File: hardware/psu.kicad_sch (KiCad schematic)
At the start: 58 parts, among them IC1 TLV61220DBVT, J2 Conn_01x03, J6 Barrel_Jack_Switch, Q3 CSD87503Q3E, Q4 CSD87503Q3E, U4 TPS63020DSJR, U5 BQ25798RQMR

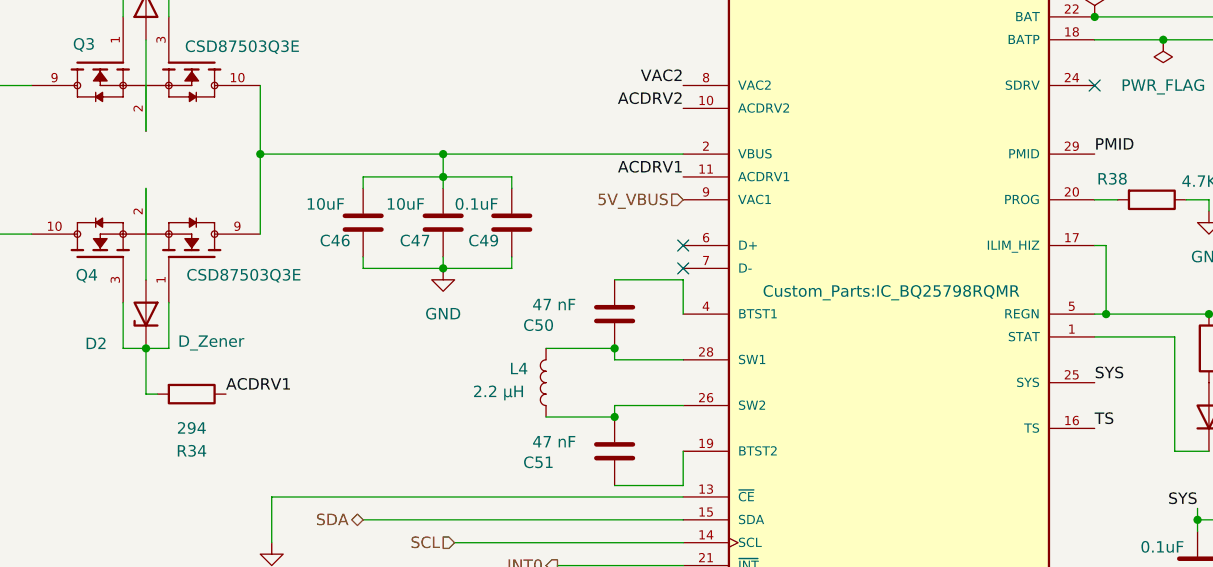
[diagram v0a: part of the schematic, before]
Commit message: updated major symbol and footprints
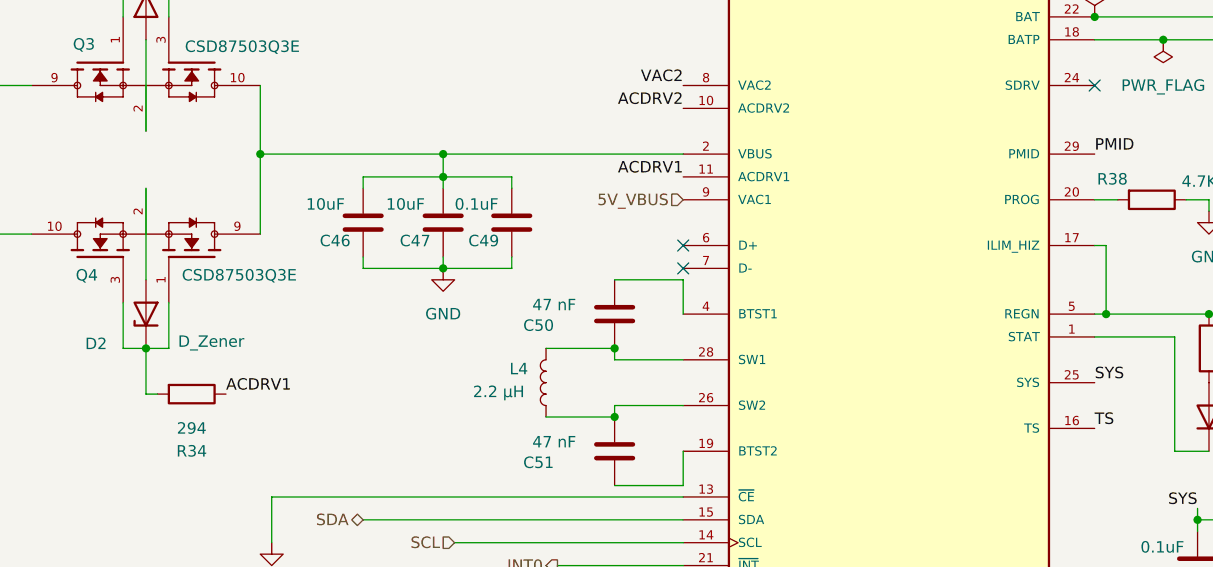
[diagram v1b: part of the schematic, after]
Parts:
- IC1: footprint (none) -> pyronet_footprints:SOT95P280X110-6; symbol TLV61220DBVT:TLV61220DBVT -> pyronet_symbols:TLV61220DBVT; Purchase-URL (none) -> https://www.snapeda.com/api/url_track_click_mouser/?unipart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
- Q3, Q4: footprint Custom_Parts:TRANS_CSD87503Q3E -> pyronet_footprints:TRANS_CSD87503Q3ET; symbol CSD87503Q3E:CSD87503Q3E -> pyronet_symbols:CSD87503Q3ET; Availability In Stock -> Warning; Check_prices https://www.snapeda.com/parts/CSD87503Q3E/Texas+Instruments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 -> https://www.snapeda.com/parts/CSD87503Q3ET/Texas+Instrument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; DigiKey_Part_Number (none) -> 296-47497-1-ND; MP CSD87503Q3E -> CSD87503Q3ET; Purchase-URL (none) -> https://www.snapeda.com/api/url_track_click_mouser/?unipart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; SnapEDA_Link https://www.snapeda.com/parts/CSD87503Q3E/Texas+Instruments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 -> https://www.snapeda.com/parts/CSD87503Q3ET/Texas+Instrument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
- U4: footprint TPS63020DSJR:IC_TPS63020DSJR -> pyronet_footprints:IC_TPS63020DSJR; symbol TPS63020DSJR:TPS63020DSJR -> pyronet_symbols:TPS63020DSJR; Purchase-URL (none) -> https://www.snapeda.com/api/url_track_click_mouser/?unipart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
- U5: footprint Custom_Parts:IC_BQ25798RQMR -> pyronet_footprints:IC_BQ25798RQMR; symbol BQ25798RQMR:BQ25798RQMR -> pyronet_symbols:BQ25798RQMR
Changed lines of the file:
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@@
 	)
 	(symbol
-		(lib_id "TLV61220DBVT:TLV61220DBVT")
+		(lib_id "pyronet_symbols:TLV61220DBVT")
 		(at 199.39 140.97 0)
 		(unit 1)
@@
 			)
 		)
-		(property "Footprint" ""
+		(property "Footprint" "pyronet_footprints:SOT95P280X110-6"
 			(at 199.39 140.97 0)
 			(effects
@@
 			)
 		)
-		(property "Description" ""
+		(property "Description" "Texas Instruments TLV61220DBVT, Boost Converter, Boost Converter 200mA Adjustable, 1.8  5.5 V, 6-Pin SOT-23"
 			(at 199.39 140.97 0)
 			(effects
@@
 					(size 1.27 1.27)
 				)
+				(justify bottom)
 				(hide yes)
 			)
@@
 			)
 		)
+		(property "Purchase-URL" "https://www.snapeda.com/api/url_track_click_mouser/?unipart_id=50780&manufacturer=Texas Instruments&part_name=TLV61220DBVT&search_term=  tlv61220dbvt"
+			(at 199.39 140.97 0)
+			(effects
+				(font
+					(size 1.27 1.27)
+				)
+				(justify bottom)
+				(hide yes)
+			)
+		)
 		(pin "6"
 		)
@@
 	)
 	(symbol
-		(lib_id "CSD87503Q3E:CSD87503Q3E")
+		(lib_name "CSD87503Q3ET_1")
+		(lib_id "pyronet_symbols:CSD87503Q3ET")
 		(at 71.12 33.02 0)
 		(unit 1)
@@
 			)
 		)
-		(property "Footprint" "Custom_Parts:TRANS_CSD87503Q3E"
+		(property "Footprint" "pyronet_footprints:TRANS_CSD87503Q3ET"
 			(at 71.12 33.02 0)
 			(effects
@@
 			)
 		)
-		(property "Check_prices" "https://www.snapeda.com/parts/CSD87503Q3E/Texas+Instruments/view-part/?ref=eda"
+		(property "Check_prices" "https://www.snapeda.com/parts/CSD87503Q3ET/Texas+Instruments/view-part/?ref=eda"
 			(at 71.12 33.02 0)
 			(effects
@@
 			)
 		)
-		(property "SnapEDA_Link" "https://www.snapeda.com/parts/CSD87503Q3E/Texas+Instruments/view-part/?ref=snap"
+		(property "SnapEDA_Link" "https://www.snapeda.com/parts/CSD87503Q3ET/Texas+Instruments/view-part/?ref=snap"
 			(at 71.12 33.02 0)
 			(effects
@@
 			)
 		)
-		(property "MP" "CSD87503Q3E"
+		(property "MP" "CSD87503Q3ET"
 			(at 71.12 33.02 0)
 			(effects
@@
 			)
 		)
-		(property "Availability" "In Stock"
+		(property "Availability" "Warning"
 			(at 71.12 33.02 0)
 			(effects
@@
 			)
 		)
+		(property "Purchase-URL" "https://www.snapeda.com/api/url_track_click_mouser/?unipart_id=1406469&manufacturer=Texas Instruments&part_name=CSD87503Q3ET&search_term=csd87503q3e"
+			(at 71.12 33.02 0)
+			(effects
+				(font
+					(size 1.27 1.27)
+				)
+				(justify bottom)
+				(hide yes)
+			)
+		)
+		(property "DigiKey_Part_Number" "296-47497-1-ND"
+			(at 71.12 33.02 0)
+			(effects
+				(font
+					(size 1.27 1.27)
+				)
+				(justify bottom)
+				(hide yes)
+			)
+		)
 		(pin "4"
 		)
@@
 	)
 	(symbol
-		(lib_id "CSD87503Q3E:CSD87503Q3E")
+		(lib_id "pyronet_symbols:CSD87503Q3ET")
 		(at 71.12 54.61 180)
 		(unit 1)
@@
 		)
 		(property "Value" "CSD87503Q3E"
-			(at 88.392 56.642 0)
+			(at 87.884 56.642 0)
 			(effects
 				(font
@@
 			)
 		)
-		(property "Footprint" "Custom_Parts:TRANS_CSD87503Q3E"
+		(property "Footprint" "pyronet_footprints:TRANS_CSD87503Q3ET"
 			(at 71.12 54.61 0)
 			(effects
@@
 			)
 		)
-		(property "Check_prices" "https://www.snapeda.com/parts/CSD87503Q3E/Texas+Instruments/view-part/?ref=eda"
+		(property "Check_prices" "https://www.snapeda.com/parts/CSD87503Q3ET/Texas+Instruments/view-part/?ref=eda"
 			(at 71.12 54.61 0)
 			(effects
@@
 			)
 		)
-		(property "SnapEDA_Link" "https://www.snapeda.com/parts/CSD87503Q3E/Texas+Instruments/view-part/?ref=snap"
+		(property "SnapEDA_Link" "https://www.snapeda.com/parts/CSD87503Q3ET/Texas+Instruments/view-part/?ref=snap"
 			(at 71.12 54.61 0)
 			(effects
@@
 			)
 		)
-		(property "MP" "CSD87503Q3E"
+		(property "MP" "CSD87503Q3ET"
 			(at 71.12 54.61 0)
 			(effects
@@
 			)
 		)
-		(property "Availability" "In Stock"
+		(property "Availability" "Warning"
 			(at 71.12 54.61 0)
 			(effects
@@
 			)
 		)
+		(property "Purchase-URL" "https://www.snapeda.com/api/url_track_click_mouser/?unipart_id=1406469&manufacturer=Texas Instruments&part_name=CSD87503Q3ET&search_term=csd87503q3e"
+			(at 71.12 54.61 0)
+			(effects
+				(font
+					(size 1.27 1.27)
+				)
+				(justify bottom)
+				(hide yes)
+			)
+		)
+		(property "DigiKey_Part_Number" "296-47497-1-ND"
+			(at 71.12 54.61 0)
+			(effects
+				(font
+					(size 1.27 1.27)
+				)
+				(justify bottom)
+				(hide yes)
+			)
+		)
 		(pin "4"
 		)
@@
 	)
 	(symbol
-		(lib_id "BQ25798RQMR:BQ25798RQMR")
+		(lib_id "pyronet_symbols:BQ25798RQMR")
 		(at 153.67 60.96 0)
 		(unit 1)
@@
 			)
 		)
-		(property "Footprint" "Custom_Parts:IC_BQ25798RQMR"
-			(at 153.924 59.182 0)
+		(property "Footprint" "pyronet_footprints:IC_BQ25798RQMR"
+			(at 153.67 60.96 0)
 			(effects
 				(font
@@
 				)
 				(justify bottom)
+				(hide yes)
 			)
 		)
@@
 	)
 	(symbol
-		(lib_id "TPS63020DSJR:TPS63020DSJR")
+		(lib_id "pyronet_symbols:TPS63020DSJR")
 		(at 57.15 152.4 0)
 		(unit 1)
@@
 			)
 		)
-		(property "Footprint" "TPS63020DSJR:IC_TPS63020DSJR"
+		(property "Footprint" "pyronet_footprints:IC_TPS63020DSJR"
 			(at 57.15 152.4 0)
 			(effects
@@
 			(at 57.15 152.4 0)
 			(effects
+				(font
+					(size 1.27 1.27)
+				)
+				(justify bottom)
+				(hide yes)
+			)
+		)
+		(property "Purchase-URL" "https://www.snapeda.com/api/url_track_click_mouser/?unipart_id=296571&manufacturer=Texas Instruments&part_name=TPS63020DSJR&search_term=tps63020dsjr"
+			(at 57.15 152.4 0)
+			(effects

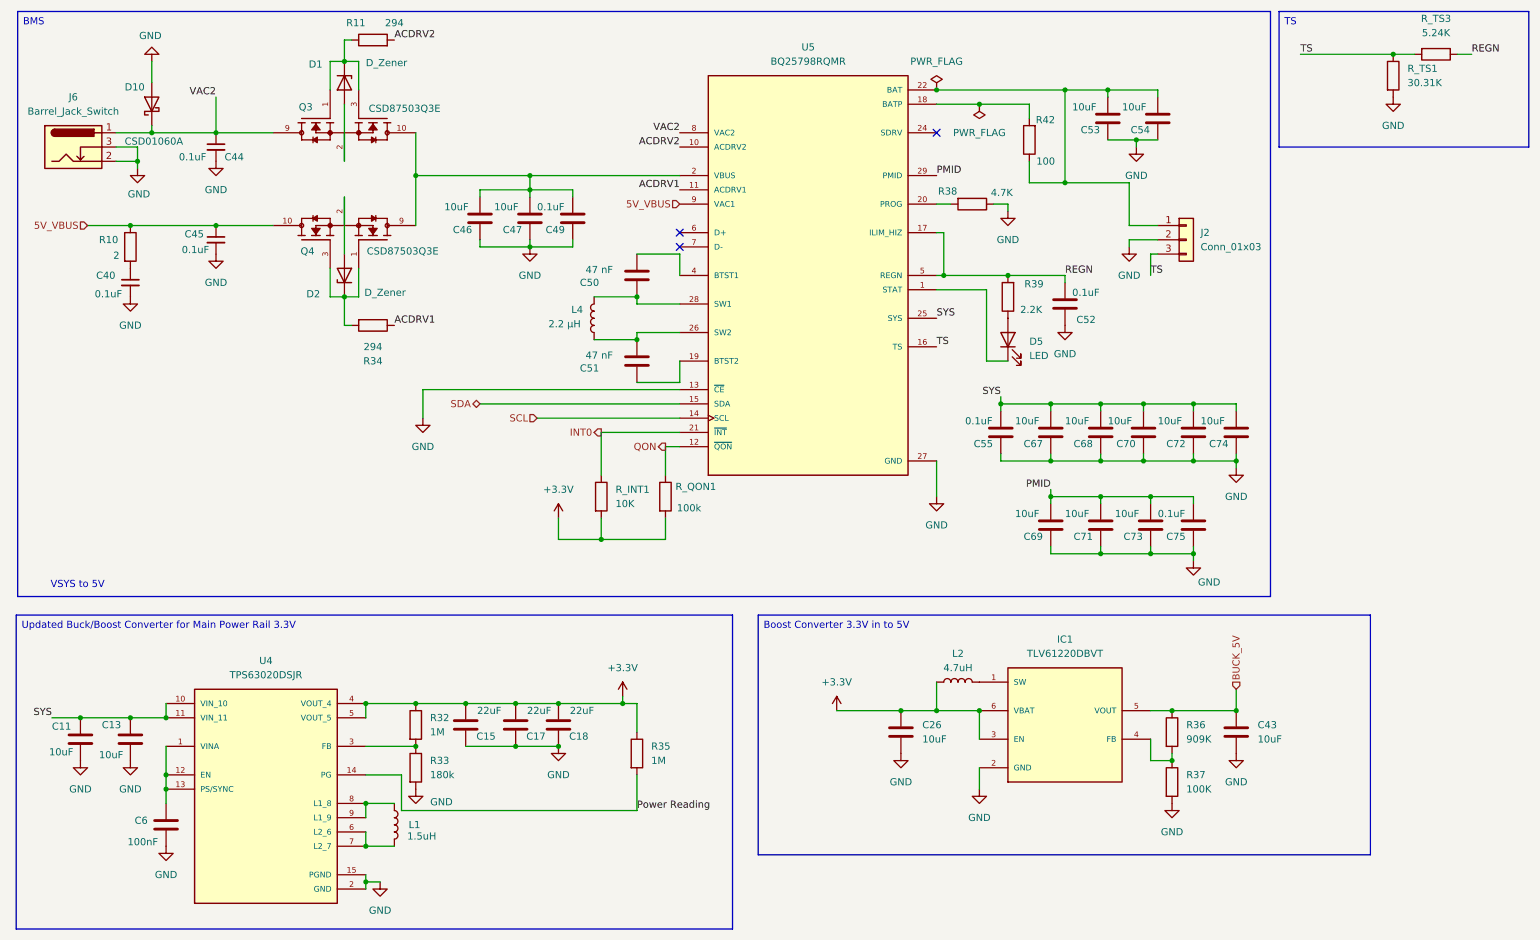
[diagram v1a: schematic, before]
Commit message: updated 5V power and pin
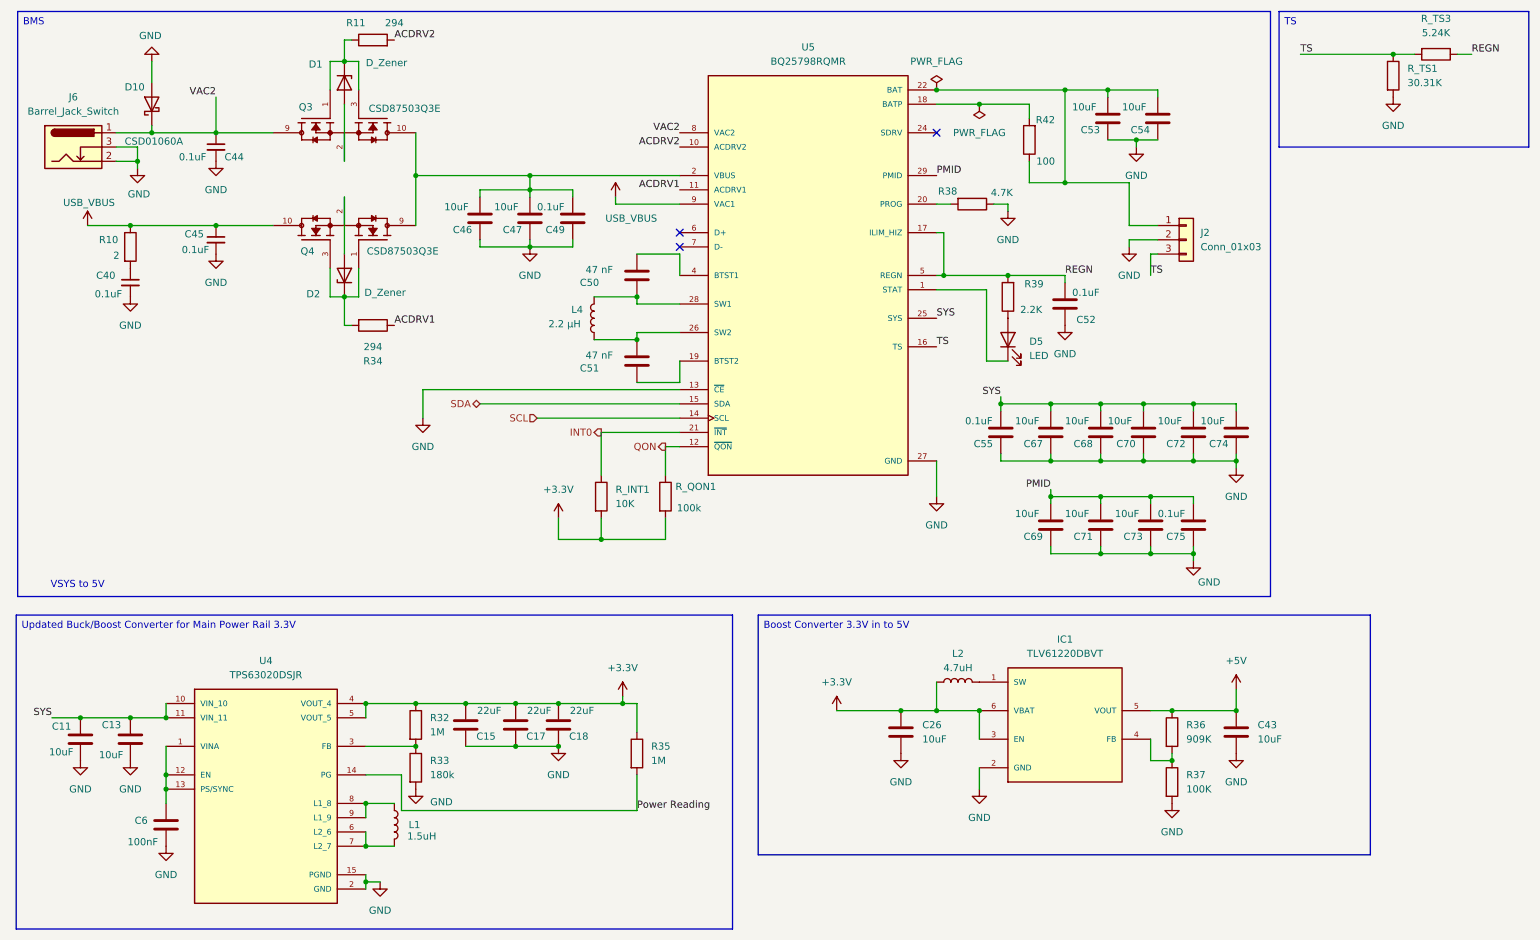
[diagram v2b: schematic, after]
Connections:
- net 5V_VBUS renamed USB_VBUS
- net BUCK_5V renamed +5V
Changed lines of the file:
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@@
 	(wire
 		(pts
+			(xy 119.38 48.26) (xy 130.81 48.26)
+		)
+		(stroke
+			(width 0)
+			(type default)
+		)
+	)
+	(wire
+		(pts
 			(xy 109.22 107.95) (xy 116.84 107.95)
 		)
@@
 	(wire
 		(pts
+			(xy 119.38 46.99) (xy 119.38 48.26)
+		)
+		(stroke
+			(width 0)
+			(type default)
+		)
+	)
+	(wire
+		(pts
 			(xy 39.37 144.78) (xy 39.37 149.86)
 		)
@@
 		)
 	)
-	(hierarchical_label "BUCK_5V"
-		(shape input)
-		(at 229.87 134.62 90)
-		(effects
-			(font
-				(size 1.27 1.27)
-			)
-			(justify left)
-		)
-	)
 	(hierarchical_label "INT0"
 		(shape output)
@@
 		)
 	)
-	(hierarchical_label "5V_VBUS"
-		(shape input)
-		(at 25.4 52.07 180)
-		(effects
-			(font
-				(size 1.27 1.27)
-			)
-			(justify right)
-		)
-	)
 	(hierarchical_label "SCL"
 		(shape input)
@@
 		)
 	)
-	(hierarchical_label "5V_VBUS"
-		(shape input)
-		(at 130.81 48.26 180)
-		(effects
-			(font
-				(size 1.27 1.27)
-			)
-			(justify right)
-		)
-	)
 	(symbol
 		(lib_id "Device:C")
@@
 	)
 	(symbol
+		(lib_id "power:VBUS")
+		(at 119.38 46.99 0)
+		(unit 1)
+		(exclude_from_sim no)
+		(in_bom yes)
+		(on_board yes)
+		(dnp no)
+		(property "Reference" "#PWR090"
+			(at 119.38 50.8 0)
+			(effects
+				(font
+					(size 1.27 1.27)
+				)
+				(hide yes)
+			)
+		)
+		(property "Value" "USB_VBUS"
+			(at 122.174 50.8 0)
+			(effects
+				(font
+					(size 1.27 1.27)
+				)
+			)
+		)
+		(property "Footprint" ""
+			(at 119.38 46.99 0)
+			(effects
+				(font
+					(size 1.27 1.27)
+				)
+				(hide yes)
+			)
+		)
+		(property "Datasheet" ""
+			(at 119.38 46.99 0)
+			(effects
+				(font
+					(size 1.27 1.27)
+				)
+				(hide yes)
+			)
+		)
+		(property "Description" "Power symbol creates a global label with name \"VBUS\""
+			(at 119.38 46.99 0)
+			(effects
+				(font
+					(size 1.27 1.27)
+				)
+				(hide yes)
+			)
+		)
+		(pin "1"
+		)
+		(instances
+			(project "Senior_Design"
+				(path "/8f5928e8-0fc1-4443-a20f-3bfeb956761e/09dae378-4d12-4dca-bc21-c216f94ec21f"
+					(reference "#PWR090")
+					(unit 1)
+				)
+			)
+		)
+	)
+	(symbol
 		(lib_id "power:PWR_FLAG")
 		(at 176.53 27.94 0)
@@
 	)
 	(symbol
+		(lib_id "power:VBUS")
+		(at 25.4 52.07 0)
+		(unit 1)
+		(exclude_from_sim no)
+		(in_bom yes)
+		(on_board yes)
+		(dnp no)
+		(property "Reference" "#PWR089"
+			(at 25.4 55.88 0)
+			(effects
+				(font
+					(size 1.27 1.27)
+				)
+				(hide yes)
+			)
+		)
+		(property "Value" "USB_VBUS"
+			(at 25.654 48.006 0)
+			(effects
+				(font
+					(size 1.27 1.27)
+				)
+			)
+		)
+		(property "Footprint" ""
+			(at 25.4 52.07 0)
+			(effects
+				(font
+					(size 1.27 1.27)
+				)
+				(hide yes)
+			)
+		)
+		(property "Datasheet" ""
+			(at 25.4 52.07 0)
+			(effects
+				(font
+					(size 1.27 1.27)
+				)
+				(hide yes)
+			)
+		)
+		(property "Description" "Power symbol creates a global label with name \"VBUS\""
+			(at 25.4 52.07 0)
+			(effects
+				(font
+					(size 1.27 1.27)
+				)
+				(hide yes)
+			)
+		)
+		(pin "1"
+		)
+		(instances
+			(project "Senior_Design"
+				(path "/8f5928e8-0fc1-4443-a20f-3bfeb956761e/09dae378-4d12-4dca-bc21-c216f94ec21f"
+					(reference "#PWR089")
+					(unit 1)
+				)
+			)
+		)
+	)
+	(symbol
 		(lib_id "power:GND")
 		(at 33.02 147.32 0)
@@
 					(unit 1)
 				)
+			)
+		)
+	)
+	(symbol
+		(lib_id "power:+5V")
+		(at 229.87 134.62 0)
+		(unit 1)
+		(exclude_from_sim no)
+		(in_bom yes)
+		(on_board yes)
+		(dnp no)
+		(fields_autoplaced yes)
+		(property "Reference" "#PWR091"
+			(at 229.87 138.43 0)
+			(effects
+				(font
+					(size 1.27 1.27)
+				)
+				(hide yes)
+			)
+		)
+		(property "Value" "+5V"
+			(at 229.87 129.54 0)
+			(effects
+				(font
+					(size 1.27 1.27)
+				)
+			)
+		)
+		(property "Footprint" ""
+			(at 229.87 134.62 0)
+			(effects
+				(font
+					(size 1.27 1.27)
+				)
+				(hide yes)
+			)
+		)
+		(property "Datasheet" ""
+			(at 229.87 134.62 0)
+			(effects
+				(font
+					(size 1.27 1.27)
+				)
+				(hide yes)
+			)
+		)
+		(property "Description" "Power symbol creates a global label with name \"+5V\""
+			(at 229.87 134.62 0)
+			(effects
+				(font
+					(size 1.27 1.27)
+				)
+				(hide yes)
+			)
+		)
+		(pin "1"
+		)
+		(instances
+			(project ""
+				(path "/8f5928e8-0fc1-4443-a20f-3bfeb956761e/09dae378-4d12-4dca-bc21-c216f94ec21f"
+					(reference "#PWR091")
+					(unit 1)
+				)

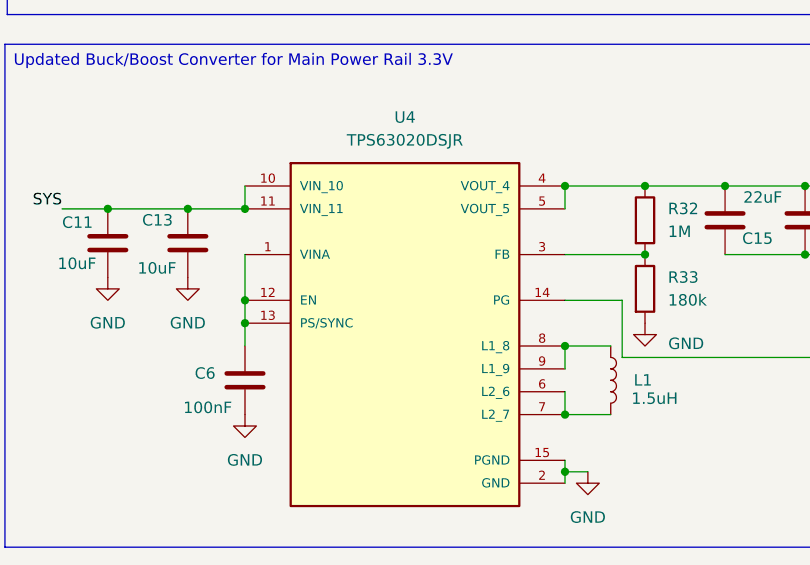
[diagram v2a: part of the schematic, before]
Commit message: passing ERC w/ exclusions
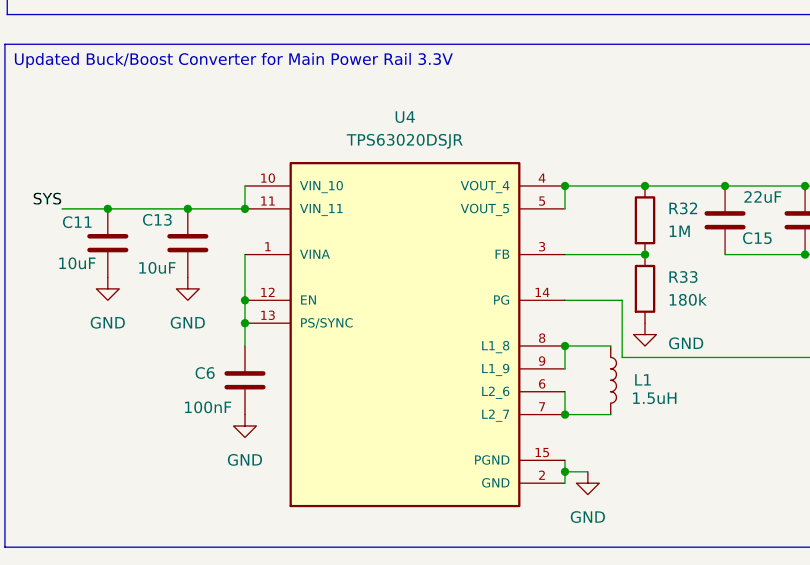
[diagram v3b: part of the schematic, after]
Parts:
- U4: footprint pyronet_footprints:IC_TPS63020DSJR -> TPS63020DSJR:IC_TPS63020DSJR
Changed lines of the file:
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@@
 			)
 		)
-		(property "Footprint" "pyronet_footprints:IC_TPS63020DSJR"
+		(property "Footprint" "TPS63020DSJR:IC_TPS63020DSJR"
 			(at 57.15 152.4 0)
 			(effects

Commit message: updated annotations
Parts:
- renumbered C11 to C301, C40 to C302, C13 to C303, C6 to C304, C44 to C305, C45 to C306, C15 to C307, C46 to C308, C17 to C309, C47 to C310, C18 to C311, C49 to C312, C50 to C313, C51 to C314, C26 to C315, C55 to C316, C67 to C317, C69 to C318, C52 to C319, C68 to C320, C71 to C321, C53 to C322, C70 to C323, C73 to C324, C54 to C325, C72 to C326, C75 to C327, C74 to C328, C43 to C329, D10 to D301, D1 to D302, D2 to D303, D5 to D304, IC1 to IC301, J6 to J301, J2 to J302, L1 to L301, L4 to L302, L2 to L303, Q3 to Q301, Q4 to Q302, R10 to R301, R11 to R302, R34 to R303, R32 to R304, R33 to R305, R35 to R306, R38 to R307, R39 to R308, R42 to R309, R36 to R310, R37 to R311, R_INT1 to R_INT301, R_QON1 to R_QON301, R_TS1 to R_TS301, R_TS3 to R_TS302, U4 to U301, U5 to U302

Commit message: wip
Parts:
- added Q303: Q_NMOS, Package_TO_SOT_SMD:SOT-23_Handsoldering, symbol Device:Q_NMOS
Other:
- moved on the sheet: C301, C302, C303, C304, C305, C306, C307, C308, C309, C310, C311, C312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
